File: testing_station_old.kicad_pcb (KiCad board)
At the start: 2 copper layers, 152.7 x 77.2 mm, 21 parts, among them J1 Pt100, J2 microSD, J3 clock, J4 Pt100, J5 BME680, J6 GPS, J7 Pt100, J8 display, U1 anemometer, U2 AM2315C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

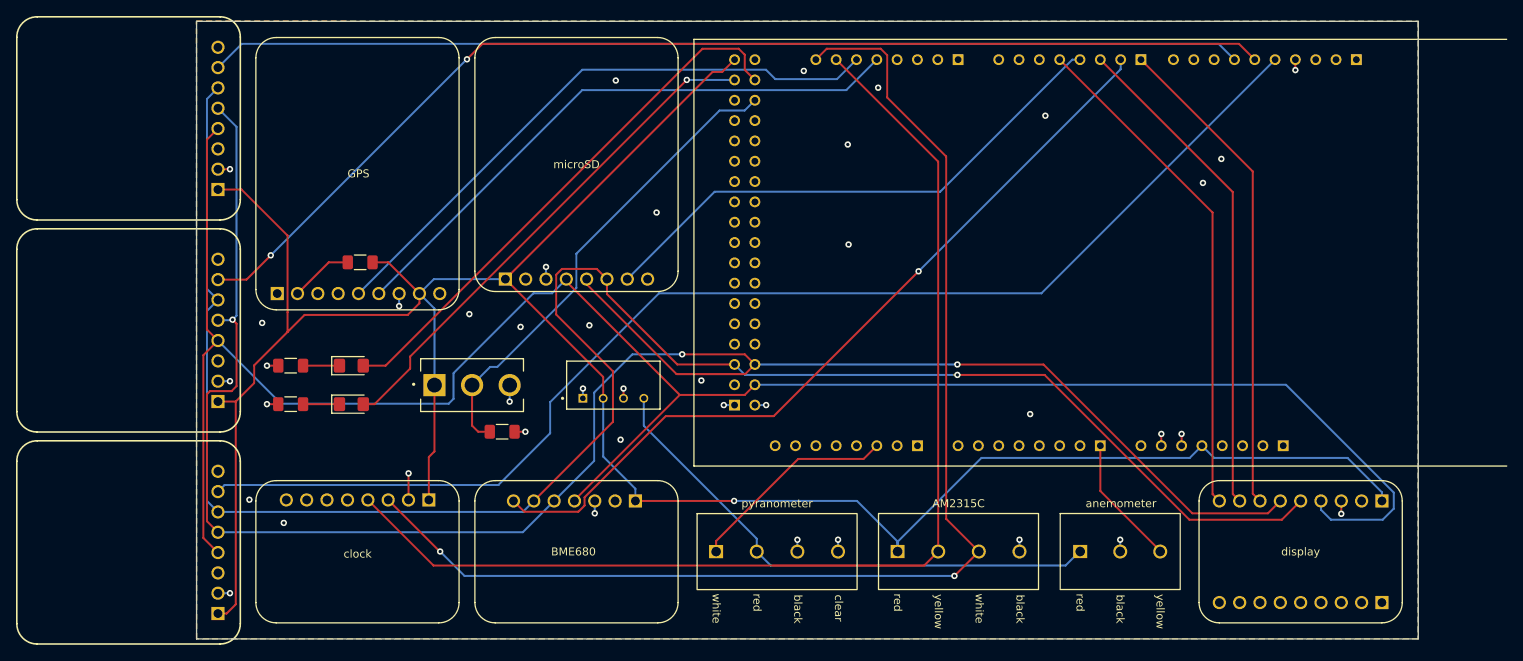
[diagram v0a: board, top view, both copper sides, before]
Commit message: added designator information in silkscreen
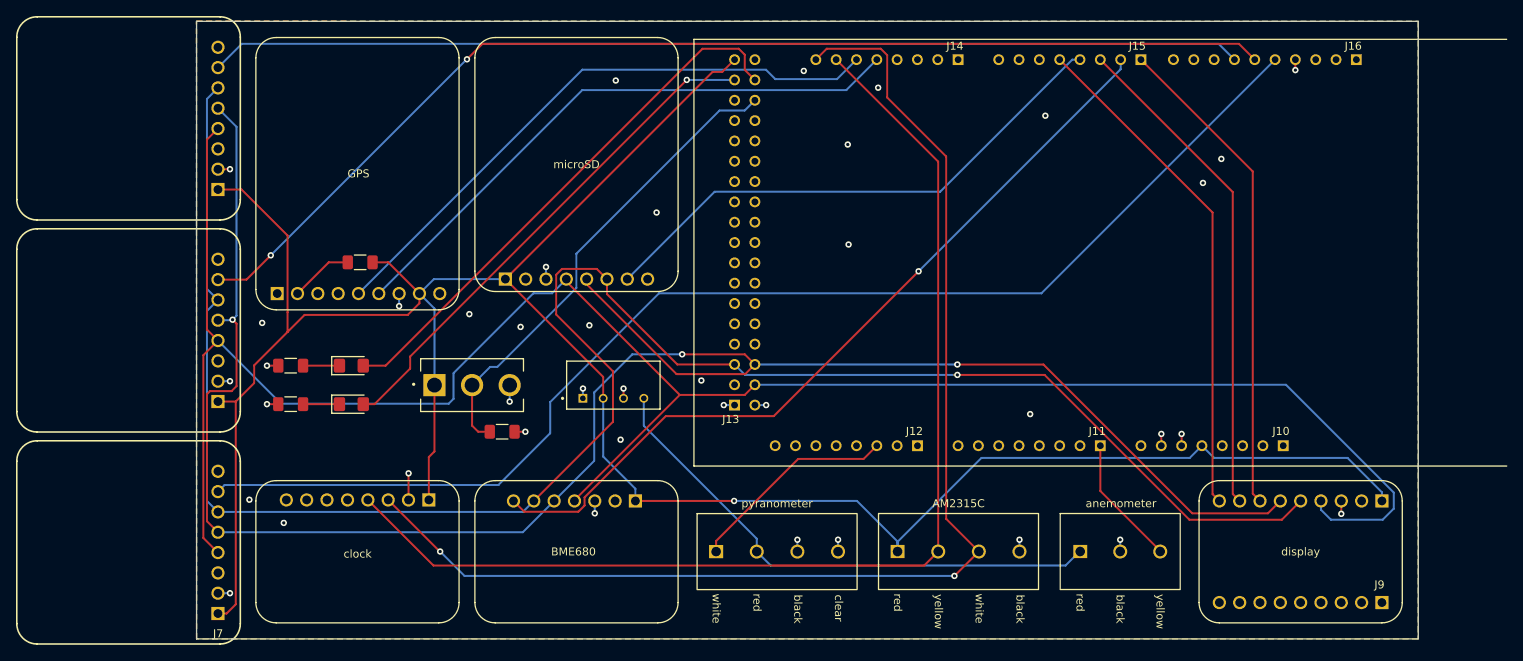
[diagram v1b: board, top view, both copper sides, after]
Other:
- board text added: "J10"
- board text added: "J11"
- board text added: "J12"
- board text added: "J13"
- board text added: "J14"
- board text added: "J15"
- board text added: "J16"
- board text added: "J9"
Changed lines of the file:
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@@
 			(unlocked yes)
 			(layer "F.SilkS")
-			(hide yes)
 			(effects
 				(font
@@
 		)
 		(property "Description" "CONN RCPT 8POS 0.1 GOLD PCB"
-			(at 61.091 145.135 0)
+			(at 61.091 145.135 180)
 			(layer "F.Fab")
 			(hide yes)
@@
 		)
 		(property "MPN" "SSQ-108-01-G-S"
-			(at 0 0 0)
+			(at 0 0 180)
 			(layer "F.Fab")
 			(hide yes)
@@
 		)
 		(property "Manufacturer" "Samtec Inc."
-			(at 0 0 0)
+			(at 0 0 180)
 			(layer "F.Fab")
 			(hide yes)
@@
 		)
 		(property "SPN" "SAM1180-08-ND"
-			(at 0 0 0)
+			(at 0 0 180)
 			(layer "F.Fab")
 			(hide yes)
@@
 		)
 		(property "Sim.Enable" "0"
-			(at 0 0 0)
+			(at 0 0 180)
 			(layer "F.Fab")
 			(hide yes)
@@
 		)
 		(property "Supplier" "Digi-Key"
-			(at 0 0 0)
+			(at 0 0 180)
 			(layer "F.Fab")
 			(hide yes)
@@
 		)
 	)
+	(gr_text "J14"
+		(at 163.82 83.67 0)
+		(layer "F.SilkS")
+		(effects
+			(font
+				(size 1 1)
+				(thickness 0.15)
+			)
+			(justify left bottom)
+		)
+	)
+	(gr_text "J9"
+		(at 217.32 151.01 0)
+		(layer "F.SilkS")
+		(effects
+			(font
+				(size 1 1)
+				(thickness 0.15)
+			)
+			(justify left bottom)
+		)
+	)
+	(gr_text "J11"
+		(at 181.61 131.82 0)
+		(layer "F.SilkS")
+		(effects
+			(font
+				(size 1 1)
+				(thickness 0.15)
+			)
+			(justify left bottom)
+		)
+	)
+	(gr_text "J15"
+		(at 186.62 83.67 0)
+		(layer "F.SilkS")
+		(effects
+			(font
+				(size 1 1)
+				(thickness 0.15)
+			)
+			(justify left bottom)
+		)
+	)
+	(gr_text "J13"
+		(at 135.8 130.33 0)
+		(layer "F.SilkS")
+		(effects
+			(font
+				(size 1 1)
+				(thickness 0.15)
+			)
+			(justify left bottom)
+		)
+	)
+	(gr_text "J12"
+		(at 158.76 131.82 0)
+		(layer "F.SilkS")
+		(effects
+			(font
+				(size 1 1)
+				(thickness 0.15)
+			)
+			(justify left bottom)
+		)
+	)
+	(gr_text "J10"
+		(at 204.58 131.82 0)
+		(layer "F.SilkS")
+		(effects
+			(font
+				(size 1 1)
+				(thickness 0.15)
+			)
+			(justify left bottom)
+		)
+	)
+	(gr_text "J16"
+		(at 213.61 83.67 0)
+		(layer "F.SilkS")
+		(effects
+			(font
+				(size 1 1)
+				(thickness 0.15)
+			)
+			(justify left bottom)
+		)
+	)

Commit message: 4pin screw terminal footprint fix
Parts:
- renumbered G*** to pic
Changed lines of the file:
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@@
 			)
 		)
-		(sheetname "Root")
-		(sheetfile "testing_station_old.kicad_sch")
 		(attr through_hole)
 		(fp_rect
@@
 			)
 		)
-		(sheetname "Root")
-		(sheetfile "testing_station_old.kicad_sch")
 		(attr through_hole)
 		(fp_rect
@@
 		(layer "B.Cu")
 		(at 86.24 84.13 180)
-		(property "Reference" "G***"
+		(property "Reference" "pic"
 			(at 7.45 -4.07 180)
 			(layer "B.SilkS")
